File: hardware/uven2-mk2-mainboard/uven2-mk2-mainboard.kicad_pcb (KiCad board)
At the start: 2 copper layers, 210 x 103 mm, 230 parts, among them J1 LEDs, J10 GND, J11 24V, J12 GND, J13 24V, J14 GND, J15 Chamber_Control, J17 PowerON/OFF, J2 1-282834-0, J3 5V, J4 GND, J5 J1B1211CCD, J6 24V, J7 GND, J8 USB_HOST, J9 24V, Q1 2N7002, Q2 2N7002, U1 DEV-16771, U10 TPS2HB50BQPWPRQ1, U11 TPS2HB50BQPWPRQ1, U12 SIDR392DP-T1-GE3, U13 SIDR392DP-T1-GE3, U14 SIDR392DP-T1-GE3, U15 SIDR392DP-T1-GE3, U16 SIDR392DP-T1-GE3, U17 SIDR392DP-T1-GE3, U18 SIDR392DP-T1-GE3, U19 SIDR392DP-T1-GE3, U2 MCP48FEB28T-20E/ST, U20 SIDR392DP-T1-GE3, U21 SIDR392DP-T1-GE3, U22 SIDR392DP-T1-GE3, U23 SIDR392DP-T1-GE3, U24 SIDR392DP-T1-GE3, U25 SIDR392DP-T1-GE3, U26 SIDR392DP-T1-GE3, U27 SIDR392DP-T1-GE3, U3 MCP48FEB28T-20E/ST, U4 TPS2HB50BQPWPRQ1, U5 TPS2HB50BQPWPRQ1, U6 TPS2HB50BQPWPRQ1, U7 TPS2HB50BQPWPRQ1, U8 TPS2HB50BQPWPRQ1, U9 TPS2HB50BQPWPRQ1

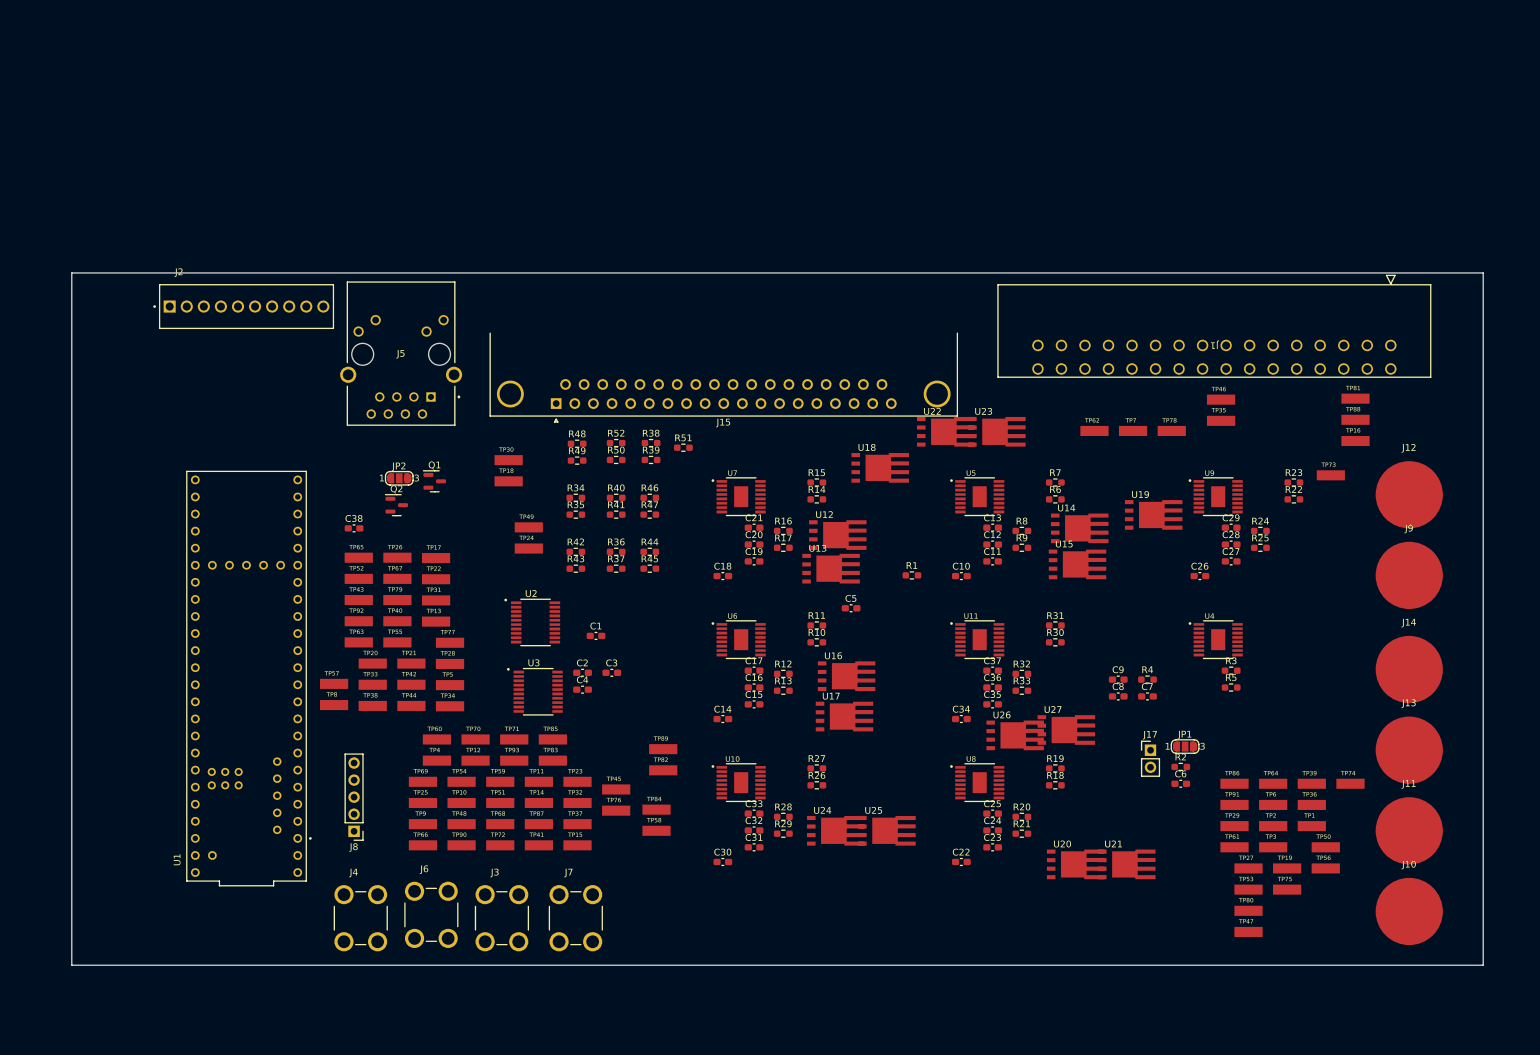
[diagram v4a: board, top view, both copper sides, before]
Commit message: layout led driver almost done
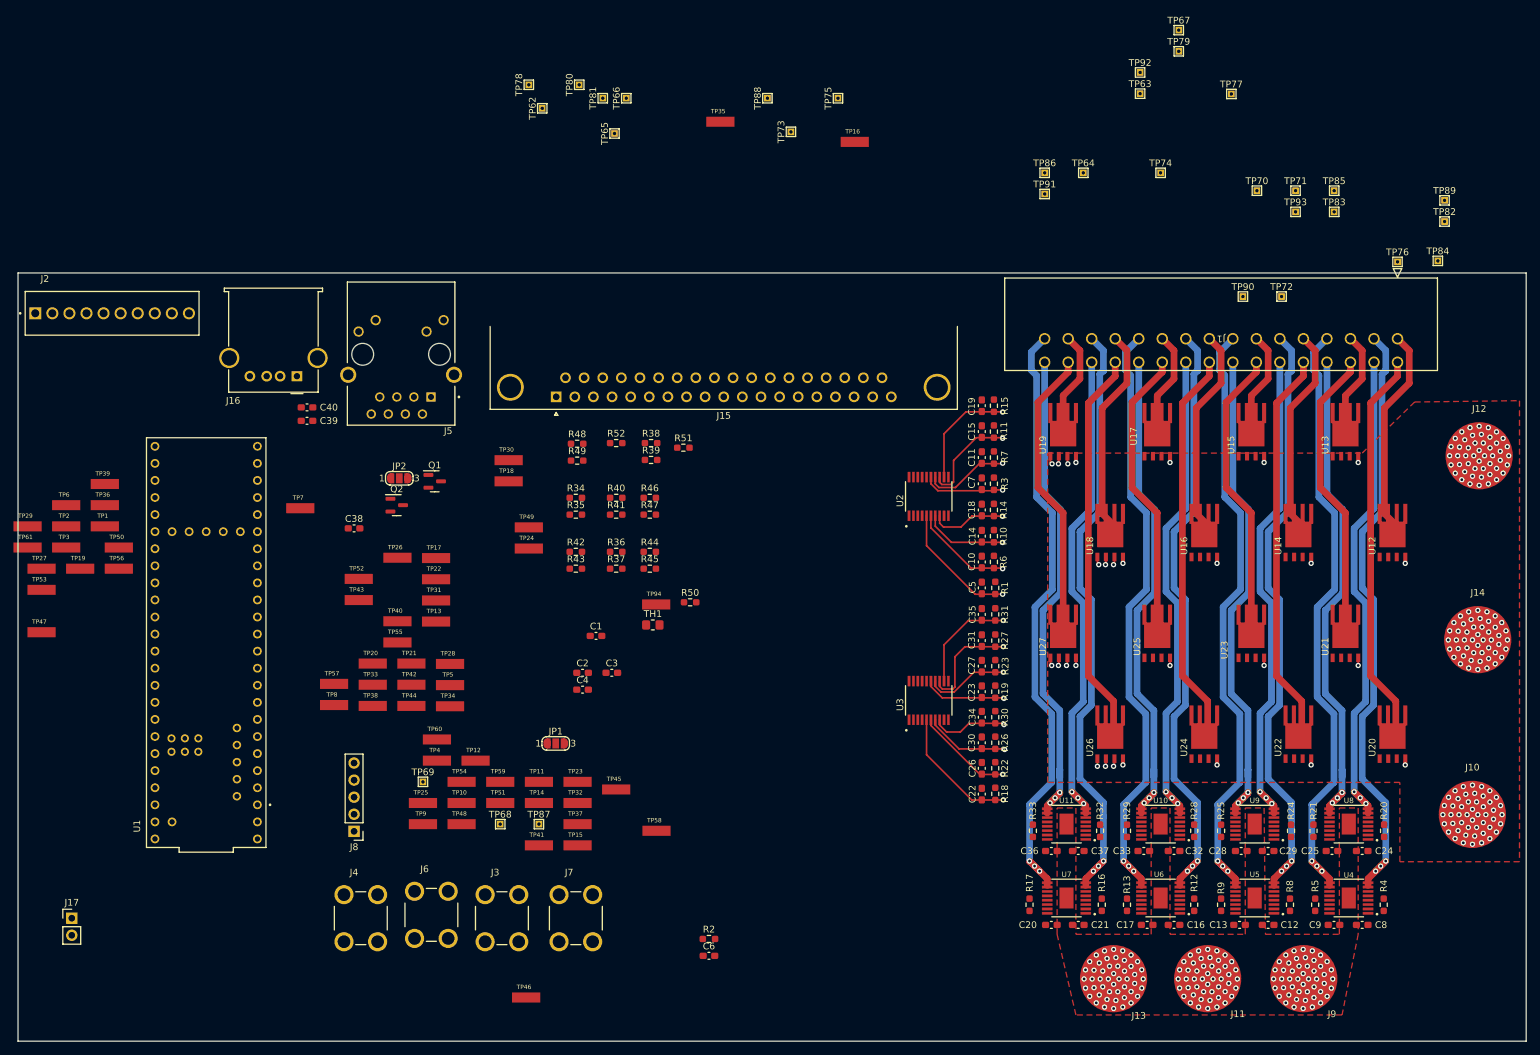
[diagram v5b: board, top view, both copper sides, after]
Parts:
- added C39: 10uF, Capacitor_SMD:C_0603_1608Metric_Pad1.08x0.95mm_HandSolder, F.Cu at (65.0, 57.0)
- added C40: 100n, Capacitor_SMD:C_0603_1608Metric_Pad1.08x0.95mm_HandSolder, F.Cu at (65.0, 55.0)
- added J16: USB_A, Connector_USB:USB_A_Molex_67643_Horizontal, F.Cu at (63.5, 50.4)
- added TH1: Thermistor_NTC, Resistor_SMD:R_0805_2012Metric_Pad1.20x1.40mm_HandSolder, F.Cu at (116.5, 87.4)
- added TP94: LED_DIAG_ENABLE_H, custom_lib:TP420X150, F.Cu at (117.0, 84.3)
- R50: value 1k -> 10k
- TP37: value LED_DIAG_ENABLE_C -> TEMP_DRIVER
- TP62, TP63, TP64, TP65, TP66, TP67, TP68, TP69, TP70, TP71, TP72, TP73, TP74, TP75, TP76, TP77, TP78, TP79, TP80, TP81, TP82, TP83, TP84, TP85, TP86, TP87, TP88, TP89, TP90, TP91, TP92, TP93: footprint custom_lib:TP420X150 -> TestPoint:TestPoint_THTPad_1.0x1.0mm_Drill0.5mm
- moved TP19 185.0 mm to (31.2, 79.0)
- moved TP27 185.0 mm to (25.5, 79.0)
- moved TP47 185.0 mm to (25.5, 88.5)
- moved TP50 185.0 mm to (37.0, 75.8)
- moved TP53 185.0 mm to (25.5, 82.2)
- moved TP56 185.0 mm to (37.0, 79.0)
- moved TP1 185.0 mm to (34.9, 72.7)
- moved TP2 185.0 mm to (29.2, 72.7)
- moved TP29 185.0 mm to (23.4, 72.7)
- moved TP3 185.0 mm to (29.2, 75.8)
- moved TP36 185.0 mm to (34.9, 69.5)
- moved TP39 185.0 mm to (34.9, 66.4)
- moved TP6 185.0 mm to (29.2, 69.5)
- moved TP61 185.0 mm to (23.4, 75.8)
- moved J17 162.4 mm to (30.0, 131.0)
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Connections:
- R50 pad 1: Net-(U1-Pad2) -> /TEMP_DRIVER
- R50 pad 2: /LED_ENABLE -> +3V3
- TP37 pad 1: /LED_DIAG_ENABLE_C -> /TEMP_DRIVER
- U1 pad 2: Net-(U1-Pad2) -> /LED_ENABLE
- U1 pad 35: /GPIO_0 -> /LED_DIAG_ENABLE_C
- U1 pad 41: /LED_DIAG_ENABLE_C -> /TEMP_DRIVER
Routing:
- net /LED7+: track 0.00 -> 90.1 mm, vias 0 -> 3
- net /LED5+: track 0.00 -> 90.1 mm, vias 0 -> 3
- net /LED1+: track 0.00 -> 90.1 mm, vias 0 -> 3
- net /LED3+: track 0.00 -> 90.1 mm, vias 0 -> 3
- net /LED0+: track 0.00 -> 89.6 mm, vias 0 -> 3
- net /LED6+: track 0.00 -> 89.6 mm, vias 0 -> 3
- net /LED4+: track 0.00 -> 89.6 mm, vias 0 -> 3
- net /LED2+: track 0.00 -> 89.6 mm, vias 0 -> 3
- net /GATE_LED8: track 0.00 -> 82.3 mm, vias 0 -> 2
- net /GATE_LED0: track 0.00 -> 81.5 mm, vias 0 -> 2
- net /LED13+: track 0.00 -> 74.4 mm, vias 0 -> 3
- net /LED9+: track 0.00 -> 74.4 mm, vias 0 -> 3
- net /LED11+: track 0.00 -> 74.4 mm, vias 0 -> 3
- net /LED15+: track 0.00 -> 74.4 mm, vias 0 -> 3
- net /LED8+: track 0.00 -> 73.1 mm, vias 0 -> 3
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- added copper zone on F.Cu, net +24V
- added copper zone on F.Cu, net GND
- added copper zone on In1.Cu, net GND
- added copper zone on In2.Cu, net GND
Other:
- board size 210 x 103 mm -> 224.4 x 114.3 mm
- copper layers 2 -> 4

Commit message: layout almost finished
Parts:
- removed JP2: Vref_select, Jumper:SolderJumper-3_P1.3mm_Open_RoundedPad1.0x1.5mm_NumberLabels
- removed TP62: LED15+, TestPoint:TestPoint_THTPad_1.0x1.0mm_Drill0.5mm
- removed TP63: LED15-, TestPoint:TestPoint_THTPad_1.0x1.0mm_Drill0.5mm
- removed TP64: LED14+, TestPoint:TestPoint_THTPad_1.0x1.0mm_Drill0.5mm
- removed TP65: LED14-, TestPoint:TestPoint_THTPad_1.0x1.0mm_Drill0.5mm
- removed TP66: LED13+, TestPoint:TestPoint_THTPad_1.0x1.0mm_Drill0.5mm
- removed TP67: LED13-, TestPoint:TestPoint_THTPad_1.0x1.0mm_Drill0.5mm
- removed TP68: LED12+, TestPoint:TestPoint_THTPad_1.0x1.0mm_Drill0.5mm
- removed TP69: LED12-, TestPoint:TestPoint_THTPad_1.0x1.0mm_Drill0.5mm
- removed TP70: LED11+, TestPoint:TestPoint_THTPad_1.0x1.0mm_Drill0.5mm
- removed TP71: LED11-, TestPoint:TestPoint_THTPad_1.0x1.0mm_Drill0.5mm
- removed TP72: LED10+, TestPoint:TestPoint_THTPad_1.0x1.0mm_Drill0.5mm
- removed TP73: LED10-, TestPoint:TestPoint_THTPad_1.0x1.0mm_Drill0.5mm
- removed TP74: LED9+, TestPoint:TestPoint_THTPad_1.0x1.0mm_Drill0.5mm
- removed TP75: LED9-, TestPoint:TestPoint_THTPad_1.0x1.0mm_Drill0.5mm
- removed TP76: LED8+, TestPoint:TestPoint_THTPad_1.0x1.0mm_Drill0.5mm
- removed TP77: LED8-, TestPoint:TestPoint_THTPad_1.0x1.0mm_Drill0.5mm
- removed TP78: LED7+, TestPoint:TestPoint_THTPad_1.0x1.0mm_Drill0.5mm
- removed TP79: LED7-, TestPoint:TestPoint_THTPad_1.0x1.0mm_Drill0.5mm
- removed TP80: LED6+, TestPoint:TestPoint_THTPad_1.0x1.0mm_Drill0.5mm
- removed TP81: LED6-, TestPoint:TestPoint_THTPad_1.0x1.0mm_Drill0.5mm
- removed TP82: LED5+, TestPoint:TestPoint_THTPad_1.0x1.0mm_Drill0.5mm
- removed TP83: LED5-, TestPoint:TestPoint_THTPad_1.0x1.0mm_Drill0.5mm
- removed TP84: LED4+, TestPoint:TestPoint_THTPad_1.0x1.0mm_Drill0.5mm
- removed TP85: LED4-, TestPoint:TestPoint_THTPad_1.0x1.0mm_Drill0.5mm
- removed TP86: LED3+, TestPoint:TestPoint_THTPad_1.0x1.0mm_Drill0.5mm
- removed TP87: LED3-, TestPoint:TestPoint_THTPad_1.0x1.0mm_Drill0.5mm
- removed TP88: LED2+, TestPoint:TestPoint_THTPad_1.0x1.0mm_Drill0.5mm
- removed TP89: LED2-, TestPoint:TestPoint_THTPad_1.0x1.0mm_Drill0.5mm
- removed TP90: LED1+, TestPoint:TestPoint_THTPad_1.0x1.0mm_Drill0.5mm
- removed TP91: LED1-, TestPoint:TestPoint_THTPad_1.0x1.0mm_Drill0.5mm
- removed TP92: LED0+, TestPoint:TestPoint_THTPad_1.0x1.0mm_Drill0.5mm
- removed TP93: LED0-, TestPoint:TestPoint_THTPad_1.0x1.0mm_Drill0.5mm
- moved TP27 191.4 mm to (206.0, 142.8), turned to -90 degrees
- moved TP28 159.1 mm to (241.6, 127.6)
- moved TP2 145.8 mm to (162.6, 131.4), turned to 180 degrees
- moved TP61 142.3 mm to (165.0, 90.2)
- moved TP53 141.7 mm to (165.2, 59.0)
- moved TP47 140.8 mm to (165.2, 71.0)
- moved TP56 132.4 mm to (165.0, 113.0)
- moved TP1 129.7 mm to (150.6, 131.4), turned to 180 degrees
- moved TP50 128.0 mm to (165.0, 78.8)
- moved J17 113.6 mm to (137.4, 94.1), turned to 90 degrees
- moved J2 113.1 mm to (85.6, 142.6)
- moved TP16 108.4 mm to (161.8, 122.8), turned to 90 degrees
- moved TP35 96.8 mm to (106.4, 107.2), turned to -90 degrees
- moved TP57 96.0 mm to (165.0, 98.0)
- moved TP52 92.6 mm to (165.1, 74.8)
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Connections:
- J15 pad 1: /TEMP_LED0 -> /TEMP_LED8
- J15 pad 14: /TEMP_LED13 -> /TEMP_LED15
- J15 pad 16: /TEMP_LED15 -> /TEMP_LED13
- J15 pad 2: /TEMP_LED1 -> /TEMP_LED7
- J15 pad 3: /TEMP_LED2 -> /TEMP_LED6
- J15 pad 4: /TEMP_LED3 -> /TEMP_LED5
- J15 pad 6: /TEMP_LED5 -> /TEMP_LED3
- J15 pad 7: /TEMP_LED6 -> /TEMP_LED2
- J15 pad 8: /TEMP_LED7 -> /TEMP_LED1
- J15 pad 9: /TEMP_LED8 -> /TEMP_LED0
- R34 pad 2: +3V3 -> +3.3V
- R35 pad 2: +3V3 -> +3.3V
- R36 pad 2: +3V3 -> +3.3V
- R37 pad 2: +3V3 -> +3.3V
- R38 pad 2: +3V3 -> +3.3V
- R39 pad 2: +3V3 -> +3.3V
- R40 pad 2: +3V3 -> +3.3V
- R41 pad 2: +3V3 -> +3.3V
- R42 pad 2: +3V3 -> +3.3V
- R43 pad 2: +3V3 -> +3.3V
- R44 pad 2: +3V3 -> +3.3V
- R45 pad 2: +3V3 -> +3.3V
- R46 pad 2: +3V3 -> +3.3V
- R47 pad 2: +3V3 -> +3.3V
- R48 pad 2: +3V3 -> +3.3V
- R49 pad 2: +3V3 -> +3.3V
- U3 pad 16: Net-(JP2-Pad2) -> Net-(JP1-Pad2)
- U3 pad 4: Net-(JP2-Pad2) -> Net-(JP1-Pad2)
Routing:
- net /LED_ENABLE: track 0.00 -> 397.0 mm, vias 0 -> 17
- net +24V: track 0.00 -> 342.7 mm
- net /LED_LATCH: track 0.00 -> 273.0 mm, vias 0 -> 12
- net +5V: track 0.00 -> 260.7 mm, vias 0 -> 1
- net /LED0_SEL: track 0.00 -> 230.2 mm, vias 0 -> 10
- net /LED1_SEL: track 0.00 -> 224.0 mm, vias 0 -> 10
- net /LED_SENS: track 0.00 -> 220.3 mm, vias 0 -> 10
- net +3.3V: track 0.00 -> 162.4 mm, vias 0 -> 2
- net /LED_DIAG_ENABLE_A: track 0.00 -> 143.5 mm, vias 0 -> 1
- net /LED_DIAG_ENABLE_B: track 0.00 -> 125.8 mm, vias 0 -> 1
- net /LED_DIAG_ENABLE_E: track 0.00 -> 113.7 mm, vias 0 -> 2
- net /MOSI: track 0.00 -> 106.8 mm, vias 0 -> 2
- net /TEMP_DRIVER: track 0.00 -> 101.9 mm, vias 0 -> 2
- net /MISO: track 0.00 -> 101.5 mm, vias 0 -> 2
- net /PowerON/OFF: track 0.00 -> 101.2 mm, vias 0 -> 1
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- added copper zone on B.Cu, net GND
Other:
- board size 224.4 x 114.3 mm -> 176.8 x 114.3 mm

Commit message: layout finished
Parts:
- added H1: MountingHole, MountingHole:MountingHole_3.2mm_M3, F.Cu at (166.0, 54.0)
- added H2: MountingHole, MountingHole:MountingHole_3.2mm_M3, F.Cu at (242.0, 144.0)
- added H3: MountingHole, MountingHole:MountingHole_3.2mm_M3, F.Cu at (106.0, 140.0)
- added H4: MountingHole, MountingHole:MountingHole_3.2mm_M3, F.Cu at (242.0, 38.0)
- added H5: MountingHole, MountingHole:MountingHole_3.2mm_M3, F.Cu at (74.7, 71.0)
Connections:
- J2 pad 5: /GPIO_0 -> GND
- J2 pad 6: GND -> +3.3V
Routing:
- net /LED_ENABLE: track 397.0 -> 451.9 mm
- net +3.3V: track 162.4 -> 211.2 mm, vias 2 -> 3
- net /ETH_TX+: track 60.0 -> 92.6 mm
- net /LED_SENS: track 220.3 -> 230.1 mm
- net /LED0_SEL: track 230.2 -> 239.5 mm
- net /LED1_SEL: track 224.0 -> 232.4 mm
- net /LED_DIAG_ENABLE_F: track 97.0 -> 93.1 mm
- net Net-(R33-Pad2): track 0.00 -> 3.76 mm
- net /GATE_LED15: track 39.2 -> 42.6 mm
- net /GATE_LED13: track 52.6 -> 55.8 mm
- net /GATE_LED7: track 40.8 -> 43.9 mm
- net /LED_DIAG_ENABLE_G: track 89.4 -> 86.3 mm
- net /GATE_LED4: track 56.6 -> 59.3 mm
- net /GATE_LED5: track 52.3 -> 55.1 mm
- net /LED_DIAG_ENABLE_E: track 113.7 -> 111.2 mm
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- added copper zone on B.Cu, net +24V
- added copper zone on F.Cu, net /LED0+
- added copper zone on F.Cu, net /LED1+
- added copper zone on F.Cu, net /LED10+
- added copper zone on F.Cu, net /LED11+
- added copper zone on F.Cu, net /LED12+
- added copper zone on F.Cu, net /LED13+
- added copper zone on F.Cu, net /LED14+
- added copper zone on F.Cu, net /LED15+
- added copper zone on F.Cu, net /LED2+
- added copper zone on F.Cu, net /LED3+
- added copper zone on F.Cu, net /LED4+
- added copper zone on F.Cu, net /LED5+
- added copper zone on F.Cu, net /LED6+
- added copper zone on F.Cu, net /LED7+
- added copper zone on F.Cu, net /LED8+
- added copper zone on F.Cu, net /LED9+
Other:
- board size 176.8 x 114.3 mm -> 176.8 x 115.3 mm
- board text added: "24V"
- board text added: "3.3V"
- board text added: "5V"
- board text added: "CHAMBER_FAN"
- board text added: "D+"
- board text added: "D-"
- board text added: "GATE_LED0"
- board text added: "GATE_LED1"
- board text added: "GATE_LED10"
- board text added: "GATE_LED11"
- board text added: "GATE_LED12"
- board text added: "GATE_LED13"
- board text added: "GATE_LED14"
- board text added: "GATE_LED15"
- board text added: "GATE_LED2"
- board text added: "GATE_LED3"
- board text added: "GATE_LED4"
- board text added: "GATE_LED5"
- board text added: "GATE_LED6"
- board text added: "GATE_LED7"
- board text added: "GATE_LED8"
- board text added: "GATE_LED9"
- board text added: "GND"
- board text added: "LATCH0"
- board text added: "LATCH1"
- board text added: "LED+"
- board text added: "LED-"
- board text added: "LED0"
- board text added: "LED0_SEL"
- board text added: "LED1"
- board text added: "LED10"
- board text added: "LED11"
- board text added: "LED12"
- board text added: "LED13"
- board text added: "LED14"
- board text added: "LED15"
- board text added: "LED1_SEL"
- board text added: "LED2"
- board text added: "LED3"
- board text added: "LED4"
- board text added: "LED5"
- board text added: "LED6"
- board text added: "LED7"
- board text added: "LED8"
- board text added: "LED9"
- board text added: "LED_DIAG_ENABLE_A"
- board text added: "LED_DIAG_ENABLE_B"
- board text added: "LED_DIAG_ENABLE_C"
- board text added: "LED_DIAG_ENABLE_D"
- board text added: "LED_DIAG_ENABLE_E"
- board text added: "LED_DIAG_ENABLE_F"
- board text added: "LED_DIAG_ENABLE_G"
- board text added: "LED_DIAG_ENABLE_H"
- board text added: "LED_ENABLE"
- board text added: "LED_FAN"
- board text added: "LED_LATCH"
- board text added: "LED_SENS"
- board text added: "POWER_ON/OFF"
- board text added: "SPI_CS0"
- board text added: "SPI_CS1"
- board text added: "SPI_MISO"
- board text added: "SPI_MOSI"
- board text added: "SPI_SCK"
- board text added: "TEMP_DRIVER"
- board text added: "TEMP_LED0"
- board text added: "TEMP_LED1"
- board text added: "TEMP_LED10"
- board text added: "TEMP_LED11"
- board text added: "TEMP_LED12"
- board text added: "TEMP_LED13"
- board text added: "TEMP_LED14"
- board text added: "TEMP_LED15"
- board text added: "TEMP_LED2"
- board text added: "TEMP_LED3"
- board text added: "TEMP_LED4"
- board text added: "TEMP_LED5"
- board text added: "TEMP_LED6"
- board text added: "TEMP_LED7"
- board text added: "TEMP_LED8"
- board text added: "TEMP_LED9"

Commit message: ordered on jlcpcb
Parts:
- added FID1: Fiducial, Fiducial:Fiducial_1mm_Dia_2.54mm_Outer_CopperTop, F.Cu at (120.0, 126.5)
- added FID2: Fiducial, Fiducial:Fiducial_1mm_Dia_2.54mm_Outer_CopperTop, F.Cu at (241.5, 136.5)
- added FID3: Fiducial, Fiducial:Fiducial_1mm_Dia_2.54mm_Outer_CopperTop, F.Cu at (165.5, 38.0)
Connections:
- J17 pad 2: unconnected-(J17-Pad2) -> GND
